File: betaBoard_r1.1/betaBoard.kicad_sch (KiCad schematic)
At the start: 40 parts, among them J1 DNP, J2 AMPHENOL_10103592-0001LF, J3 DNP, J4 DNP, J5 DNP, J6 DNP, U1 AMS1117-3.3_SOT223

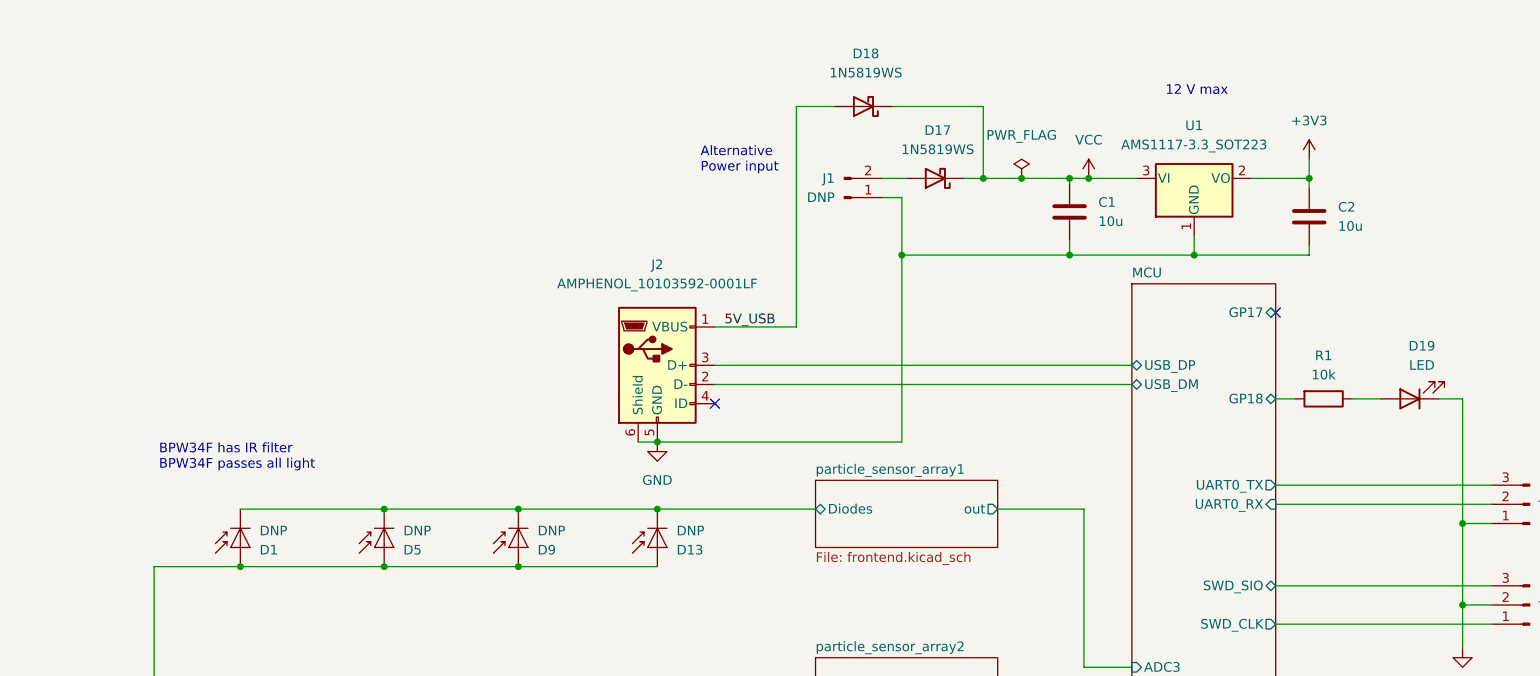
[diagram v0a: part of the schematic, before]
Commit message: move all hardware files to one folder
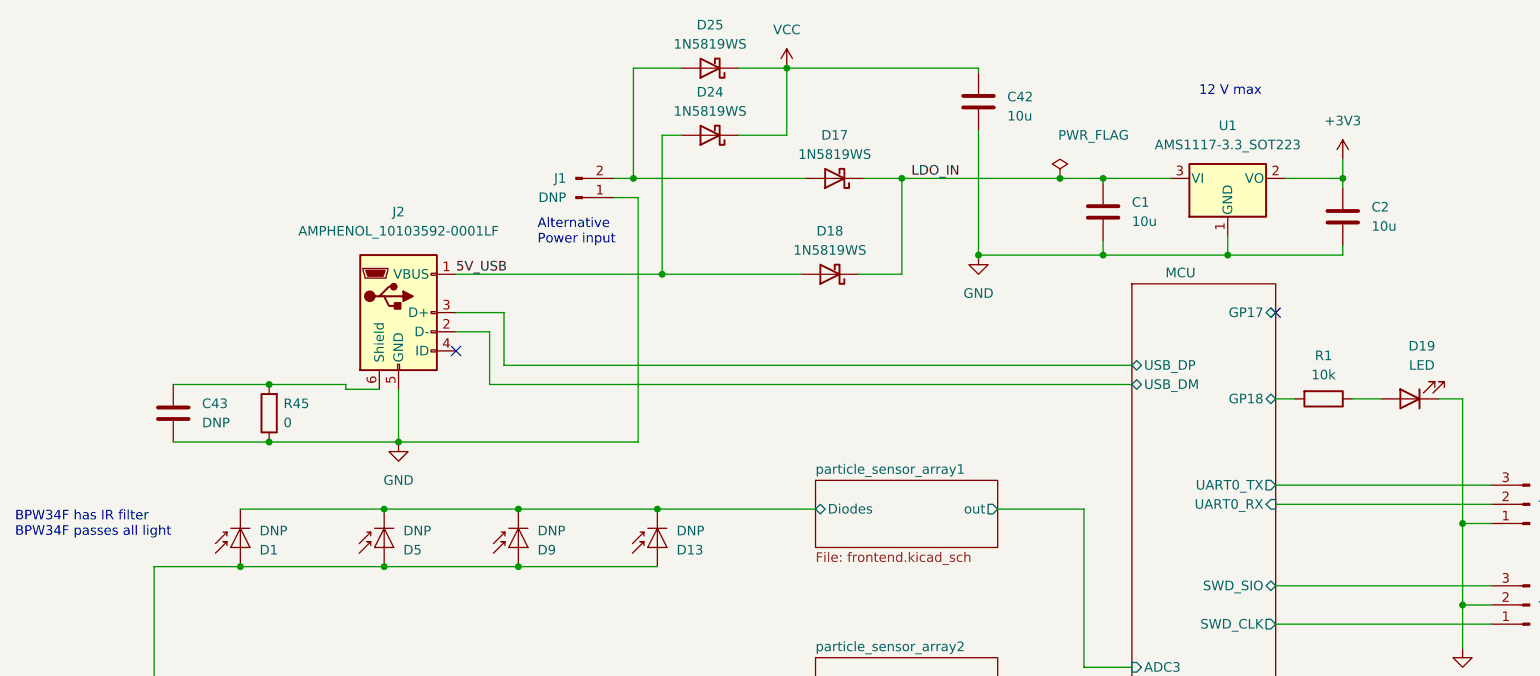
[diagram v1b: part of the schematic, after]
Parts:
- added C42: 10u, Capacitor_SMD:C_1206_3216Metric, symbol Device:C
- added C43: DNP, Capacitor_SMD:C_0603_1608Metric, symbol Device:C
- added D24, D25: 1N5819WS, Diode_SMD:D_SOD-323, symbol Diode:1N5819WS
- added R45: 0, Resistor_SMD:R_0603_1608Metric, symbol Device:R
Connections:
- net 5V_USB: now also D24.2 (A)
- net GND: now also C42.2, C43.2, R45.1; no longer J2.6 (Shield)
- net VCC: now also C42.1, D24.1 (K), D25.1 (K); no longer C1.1, D17.1 (K), D18.1 (K), U1.3 (VI)
- net at D17.2 (A), J1.2 (Pin_2): now also D25.2 (A)
- new net: C43.1, J2.6 (Shield), R45.2
- new net LDO_IN: C1.1, D17.1 (K), D18.1 (K), U1.3 (VI)
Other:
- moved on the sheet: C1, C2, D17, D18, J1, J2, U1
